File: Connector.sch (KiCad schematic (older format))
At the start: 10 parts, among them CON1 SFML_TFML-120-STACK-CON1, CON2 SFML_TFML-120-STACK-CON2

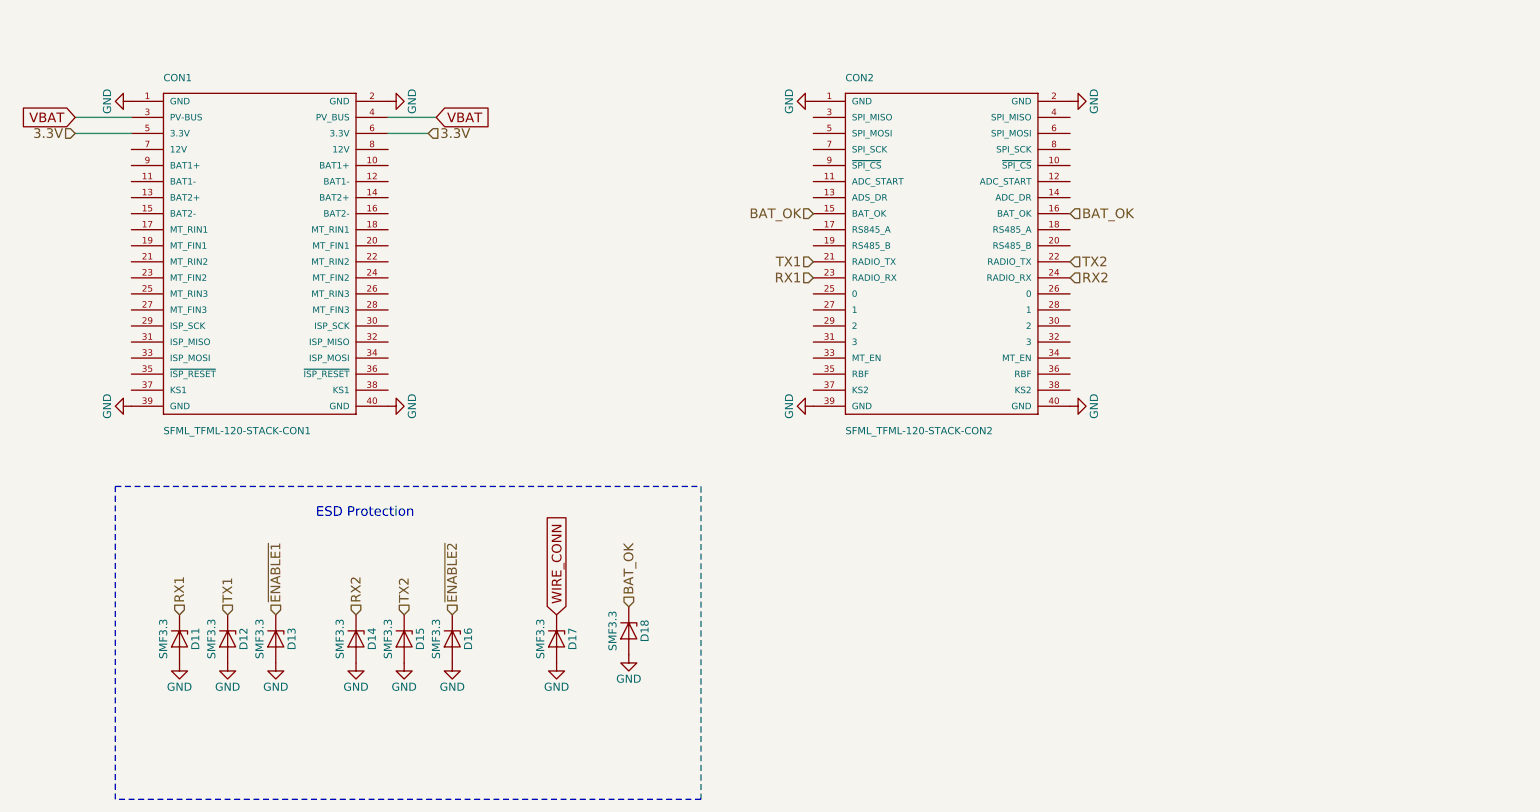
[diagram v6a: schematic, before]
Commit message: Adds Cubesat Connector to Layout
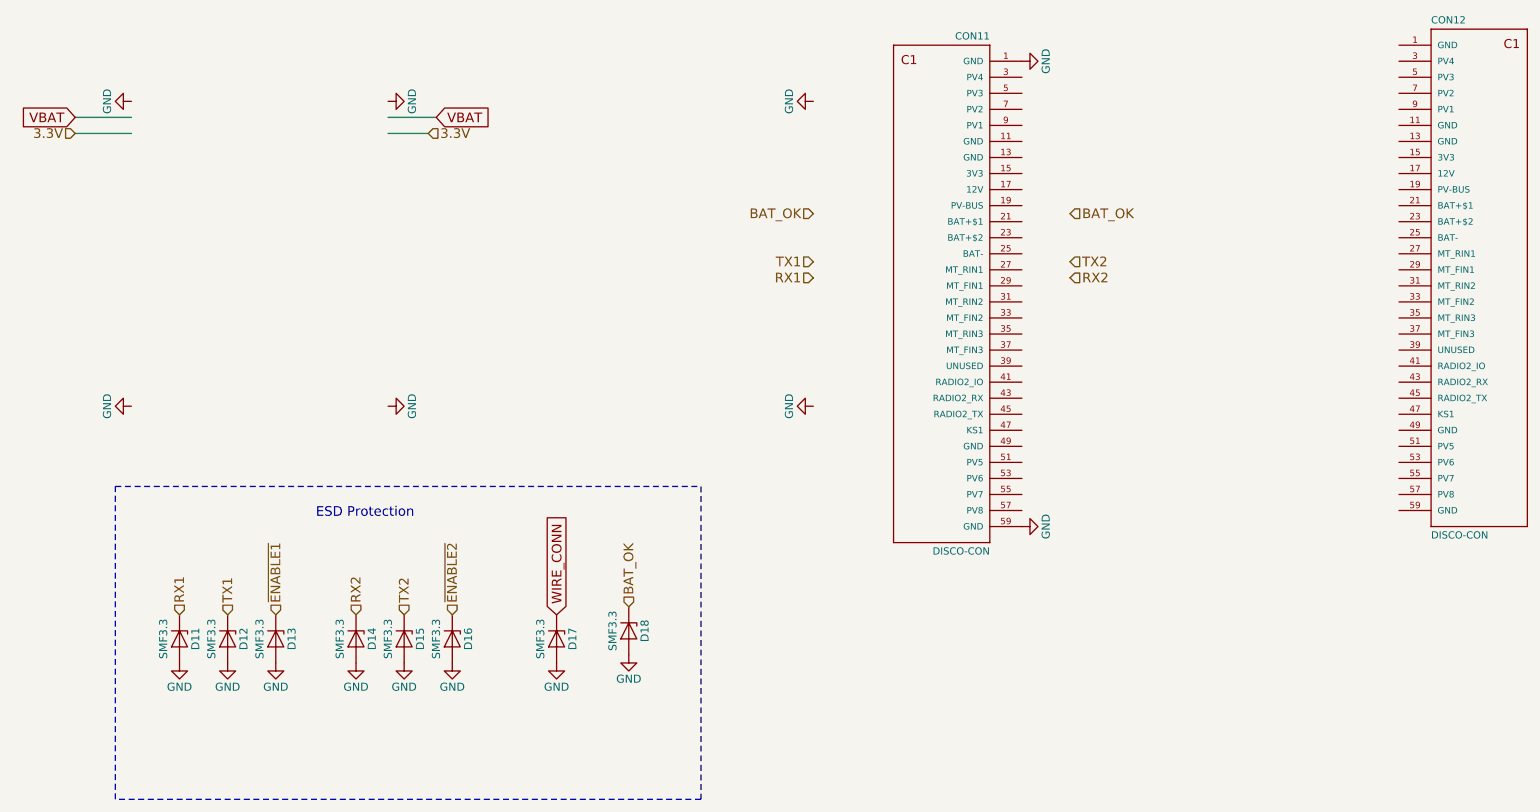
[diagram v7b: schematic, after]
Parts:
- removed CON1: SFML_TFML-120-STACK-CON1, DISCO_Connector_TFML_SFML-120-02-STACKED-A, symbol SFML_TFML-120-STACK-CON1
- removed CON2: SFML_TFML-120-STACK-CON2, DISCO_Connector_TFML_SFML-120-02-STACKED-A, symbol SFML_TFML-120-STACK-CON2
- added CON11, CON12: DISCO-CON, cubesatFunkmodul:Cubesatconnector, symbol DISCO-CON
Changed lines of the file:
@@
 LIBS:contrib
 LIBS:valves
+LIBS:nxp-ic
+LIBS:7400-ic
 LIBS:cubesatFunkmodul-cache
 LIBS:funkmodul
+LIBS:CubeSat-Bus-1
+LIBS:CubeSat-Bus-2
 EELAYER 25 0
 EELAYER END
@@
 $EndComp
 $Comp
-L GND #PWR035
+L GND #PWR37
 U 1 1 59C4523B
 P 2300 4700
-F 0 "#PWR035" H 2300 4450 50  0001 C CNN
+F 0 "#PWR37" H 2300 4450 50  0001 C CNN
 F 1 "GND" H 2300 4550 50  0000 C CNN
 F 2 "" H 2300 4700 50  0001 C CNN
@@
 $EndComp
 $Comp
-L GND #PWR036
+L GND #PWR38
 U 1 1 59C45255
 P 2600 4700
-F 0 "#PWR036" H 2600 4450 50  0001 C CNN
+F 0 "#PWR38" H 2600 4450 50  0001 C CNN
 F 1 "GND" H 2600 4550 50  0000 C CNN
 F 2 "" H 2600 4700 50  0001 C CNN
@@
 $EndComp
 $Comp
-L GND #PWR037
+L GND #PWR39
 U 1 1 59C4526F
 P 2900 4700
-F 0 "#PWR037" H 2900 4450 50  0001 C CNN
+F 0 "#PWR39" H 2900 4450 50  0001 C CNN
 F 1 "GND" H 2900 4550 50  0000 C CNN
 F 2 "" H 2900 4700 50  0001 C CNN
@@
 $EndComp
 $Comp
-L GND #PWR038
+L GND #PWR40
 U 1 1 59C452E4
 P 3400 4700
-F 0 "#PWR038" H 3400 4450 50  0001 C CNN
+F 0 "#PWR40" H 3400 4450 50  0001 C CNN
 F 1 "GND" H 3400 4550 50  0000 C CNN
 F 2 "" H 3400 4700 50  0001 C CNN
@@
 $EndComp
 $Comp
-L GND #PWR039
+L GND #PWR43
 U 1 1 59C452EA
 P 3700 4700
-F 0 "#PWR039" H 3700 4450 50  0001 C CNN
+F 0 "#PWR43" H 3700 4450 50  0001 C CNN
 F 1 "GND" H 3700 4550 50  0000 C CNN
 F 2 "" H 3700 4700 50  0001 C CNN
@@
 $EndComp
 $Comp
-L GND #PWR040
+L GND #PWR44
 U 1 1 59C452F0
 P 4000 4700
-F 0 "#PWR040" H 4000 4450 50  0001 C CNN
+F 0 "#PWR44" H 4000 4450 50  0001 C CNN
 F 1 "GND" H 4000 4550 50  0000 C CNN
 F 2 "" H 4000 4700 50  0001 C CNN
@@
 $EndComp
 $Comp
-L GND #PWR041
+L GND #PWR45
 U 1 1 59C45994
 P 4650 4700
-F 0 "#PWR041" H 4650 4450 50  0001 C CNN
+F 0 "#PWR45" H 4650 4450 50  0001 C CNN
 F 1 "GND" H 4650 4550 50  0000 C CNN
 F 2 "" H 4650 4700 50  0001 C CNN
@@
 ESD Protection
 $Comp
-L SFML_TFML-120-STACK-CON1 CON1
-U 1 1 59DA7B1E
-P 2800 2200
-F 0 "CON1" H 2200 3320 45  0000 L BNN
-F 1 "SFML_TFML-120-STACK-CON1" H 2200 1120 45  0000 L BNN
-F 2 "DISCO_Connector_TFML_SFML-120-02-STACKED-A" H 2830 2350 20  0001 C CNN
-F 3 "" H 2800 2200 60  0001 C CNN
-	1    2800 2200
-	1    0    0    -1
-$EndComp
-$Comp
-L SFML_TFML-120-STACK-CON2 CON2
-U 1 1 59DA7C3F
-P 7050 2200
-F 0 "CON2" H 6450 3320 45  0000 L BNN
-F 1 "SFML_TFML-120-STACK-CON2" H 6450 1120 45  0000 L BNN
-F 2 "DISCO_Connector_TFML_SFML-120-02-STACKED-A" H 7080 2350 20  0001 C CNN
-F 3 "" H 7050 2200 60  0001 C CNN
-	1    7050 2200
-	1    0    0    -1
-$EndComp
-$Comp
-L GND #PWR042
+L GND #PWR49
 U 1 1 59DA7E4B
-P 7850 1200
-F 0 "#PWR042" H 7850 950 50  0001 C CNN
-F 1 "GND" H 7850 1050 50  0000 C CNN
-F 2 "" H 7850 1200 50  0001 C CNN
-F 3 "" H 7850 1200 50  0001 C CNN
-	1    7850 1200
+P 7550 950
+F 0 "#PWR49" H 7550 700 50  0001 C CNN
+F 1 "GND" H 7550 800 50  0000 C CNN
+F 2 "" H 7550 950 50  0001 C CNN
+F 3 "" H 7550 950 50  0001 C CNN
+	1    7550 950
 	0    -1   -1   0
 $EndComp
 $Comp
-L GND #PWR043
+L GND #PWR47
 U 1 1 59DA7E71
 P 6250 1200
-F 0 "#PWR043" H 6250 950 50  0001 C CNN
+F 0 "#PWR47" H 6250 950 50  0001 C CNN
 F 1 "GND" H 6250 1050 50  0000 C CNN
 F 2 "" H 6250 1200 50  0001 C CNN
@@
 $EndComp
 $Comp
-L GND #PWR044
+L GND #PWR48
 U 1 1 59DA7F27
 P 6250 3100
-F 0 "#PWR044" H 6250 2850 50  0001 C CNN
+F 0 "#PWR48" H 6250 2850 50  0001 C CNN
 F 1 "GND" H 6250 2950 50  0000 C CNN
 F 2 "" H 6250 3100 50  0001 C CNN
@@
 $EndComp
 $Comp
-L GND #PWR045
+L GND #PWR50
 U 1 1 59DA7F4D
-P 7850 3100
-F 0 "#PWR045" H 7850 2850 50  0001 C CNN
-F 1 "GND" H 7850 2950 50  0000 C CNN
-F 2 "" H 7850 3100 50  0001 C CNN
-F 3 "" H 7850 3100 50  0001 C CNN
-	1    7850 3100
+P 7550 3850
+F 0 "#PWR50" H 7550 3600 50  0001 C CNN
+F 1 "GND" H 7550 3700 50  0000 C CNN
+F 2 "" H 7550 3850 50  0001 C CNN
+F 3 "" H 7550 3850 50  0001 C CNN
+	1    7550 3850
 	0    -1   -1   0
 $EndComp
 $Comp
-L GND #PWR046
+L GND #PWR41
 U 1 1 59DA801E
 P 3600 1200
-F 0 "#PWR046" H 3600 950 50  0001 C CNN
+F 0 "#PWR41" H 3600 950 50  0001 C CNN
 F 1 "GND" H 3600 1050 50  0000 C CNN
 F 2 "" H 3600 1200 50  0001 C CNN
@@
 $EndComp
 $Comp
-L GND #PWR047
+L GND #PWR35
 U 1 1 59DA8044
 P 2000 1200
-F 0 "#PWR047" H 2000 950 50  0001 C CNN
+F 0 "#PWR35" H 2000 950 50  0001 C CNN
 F 1 "GND" H 2000 1050 50  0000 C CNN
 F 2 "" H 2000 1200 50  0001 C CNN
@@
 $EndComp
 $Comp
-L GND #PWR048
+L GND #PWR36
 U 1 1 59DA8115
 P 2000 3100
-F 0 "#PWR048" H 2000 2850 50  0001 C CNN
+F 0 "#PWR36" H 2000 2850 50  0001 C CNN
 F 1 "GND" H 2000 2950 50  0000 C CNN
 F 2 "" H 2000 3100 50  0001 C CNN
@@
 $EndComp
 $Comp
-L GND #PWR049
+L GND #PWR42
 U 1 1 59DA82BE
 P 3600 3100
-F 0 "#PWR049" H 3600 2850 50  0001 C CNN
+F 0 "#PWR42" H 3600 2850 50  0001 C CNN
 F 1 "GND" H 3600 2950 50  0000 C CNN
 F 2 "" H 3600 3100 50  0001 C CNN
@@
 $EndComp
 $Comp
-L GND #PWR050
+L GND #PWR46
 U 1 1 59DAB906
 P 5100 4650
-F 0 "#PWR050" H 5100 4400 50  0001 C CNN
+F 0 "#PWR46" H 5100 4400 50  0001 C CNN
 F 1 "GND" H 5100 4500 50  0000 C CNN
 F 2 "" H 5100 4650 50  0001 C CNN
@@
 	1    0    0    -1
 $EndComp
+$Comp
+L DISCO-CON CON12
+U 1 1 59E5D7B1
+P 10400 2250
+F 0 "CON12" H 10100 3780 45  0000 L BNN
+F 1 "DISCO-CON" H 10100 570 45  0000 L BNN
+F 2 "cubesatFunkmodul:Cubesatconnector" H 10430 2400 20  0001 C CNN
+F 3 "" H 10400 2250 60  0001 C CNN
+	1    10400 2250
+	1    0    0    -1
+$EndComp
+$Comp
+L DISCO-CON CON11
+U 1 1 59E5D88F
+P 7050 2350
+F 0 "CON11" H 6750 3880 45  0000 L BNN
+F 1 "DISCO-CON" H 6750 670 45  0000 L BNN
+F 2 "cubesatFunkmodul:Cubesatconnector" H 7080 2500 20  0001 C CNN
+F 3 "" H 7050 2350 60  0001 C CNN
+	1    7050 2350
+	-1   0    0    -1
+$EndComp
 $EndSCHEMATC
